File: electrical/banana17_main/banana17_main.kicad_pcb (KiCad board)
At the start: 2 copper layers, 62 parts, among them J1 78171-0004, SW1 SW, SW10 SW, SW11 SW, SW12 SW, SW13 SW, SW14 SW, SW15 SW, SW16 SW, SW17 SW, SW2 SW, SW3 SW, SW4 SW, SW5 SW, SW6 SW, SW7 SW, SW8 SW, SW9 SW, U1 RP2040, U2 NCP1117-3.3_SOT223, U3 ssd1306_128x32, U4 W25Q128JVS, Y1 ABMB-272-T3

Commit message: Minor changes to placement of MCU.
Minor changes to placement of MCU.
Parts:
- moved R3 31.6 mm to (251.0, 101.5)
- moved C1 21.2 mm to (227.4, 114.9)
- moved C10 21.2 mm to (229.6, 114.9)
- moved C4 21.2 mm to (226.4, 114.9)
- moved C8 21.2 mm to (223.3, 122.4)
- moved C9 21.2 mm to (223.3, 118.8)
- moved R2 21.2 mm to (227.9, 111.9)
- moved Y1 21.2 mm to (232.3, 131.0)
- moved C5 21.2 mm to (236.0, 117.7)
- moved C11 21.2 mm to (225.4, 114.9)
- moved C2 21.2 mm to (230.6, 114.9)
- moved C3 21.2 mm to (228.2, 128.5)
- moved C6 21.2 mm to (236.0, 122.4)
- moved C7 21.2 mm to (229.2, 128.5)
- moved J1 21.2 mm to (228.5, 107.7)
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
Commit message: General layout complete.
General layout complete.
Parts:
- C12, C13, C14, C15, C16: footprint Capacitor_SMD:C_0805_2012Metric_Pad1.18x1.45mm_HandSolder -> Capacitor_SMD:C_0402_1005Metric_Pad0.74x0.62mm_HandSolder
- R3: footprint Resistor_SMD:R_0805_2012Metric_Pad1.20x1.40mm_HandSolder -> Resistor_SMD:R_0402_1005Metric_Pad0.72x0.64mm_HandSolder
- moved C13 73.6 mm to (179.8, 87.6)
- moved C12 71.8 mm to (184.3, 87.6), turned to 0 degrees
- moved C16 70.8 mm to (190.1, 114.3), turned to 0 degrees
- moved C15 70.1 mm to (192.8, 114.3)
- moved U2 62.9 mm to (181.4, 92.9), turned to -90 degrees
- moved C14 59.8 mm to (194.2, 90.7)
- moved R3 49.7 mm to (202.6, 90.2)
- moved U4 48.3 mm to (198.4, 94.3)
- moved BOOT_SEL1 46.6 mm to (199.6, 86.3)
- moved J1 43.8 mm to (189.9, 86.8)
- moved Y1 42.9 mm to (191.8, 116.7)
- moved C3 42.3 mm to (189.3, 111.8)
- moved C7 42.3 mm to (190.3, 111.8)
- moved C1 41.9 mm to (188.8, 98.5)
- moved C10 41.9 mm to (191.0, 98.5)
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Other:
- board outline added: 110 x 110 mm

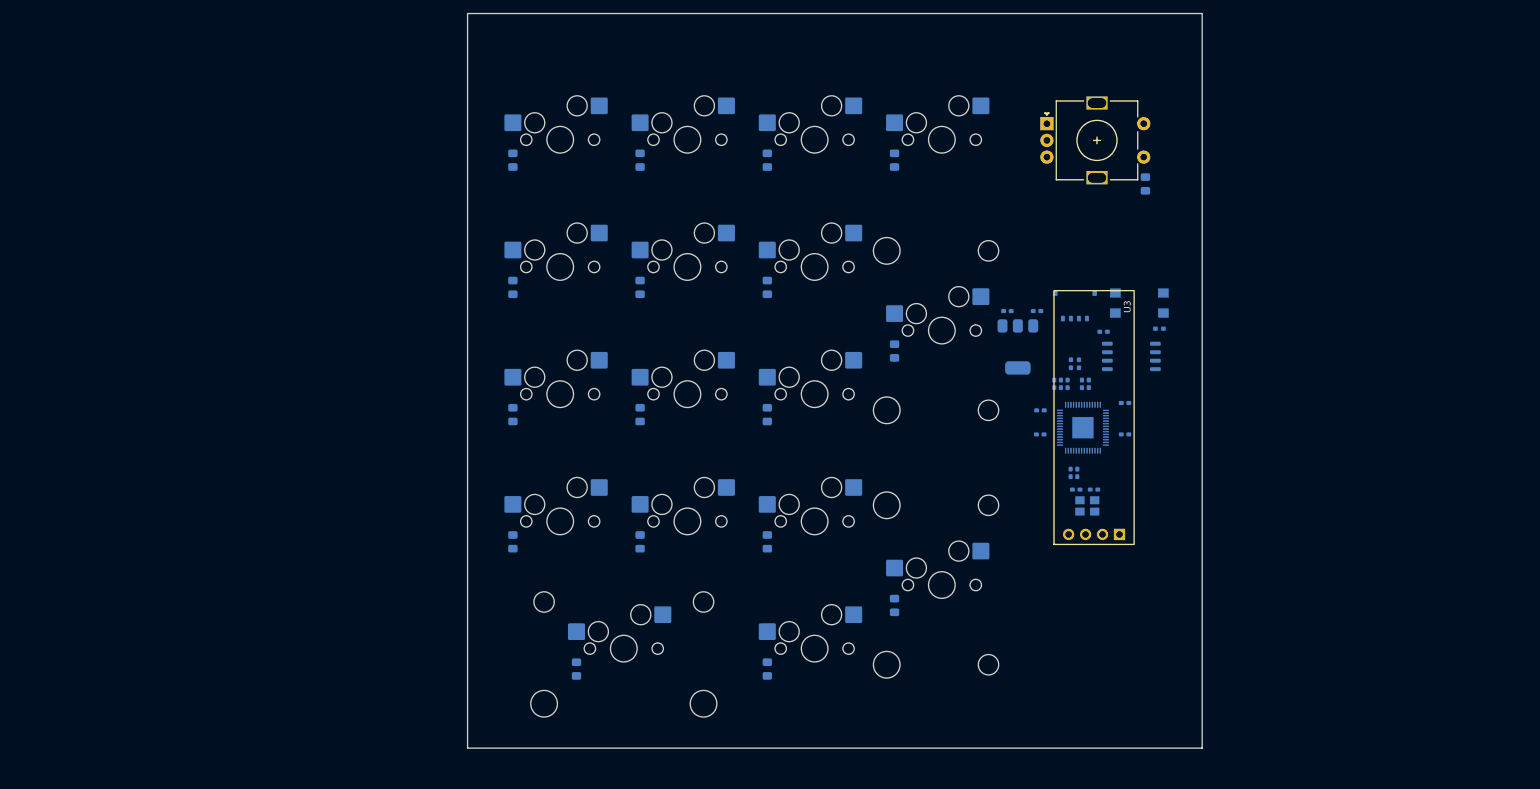
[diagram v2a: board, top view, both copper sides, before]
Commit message: Added second rotary encoder.
Added second rotary encoder.
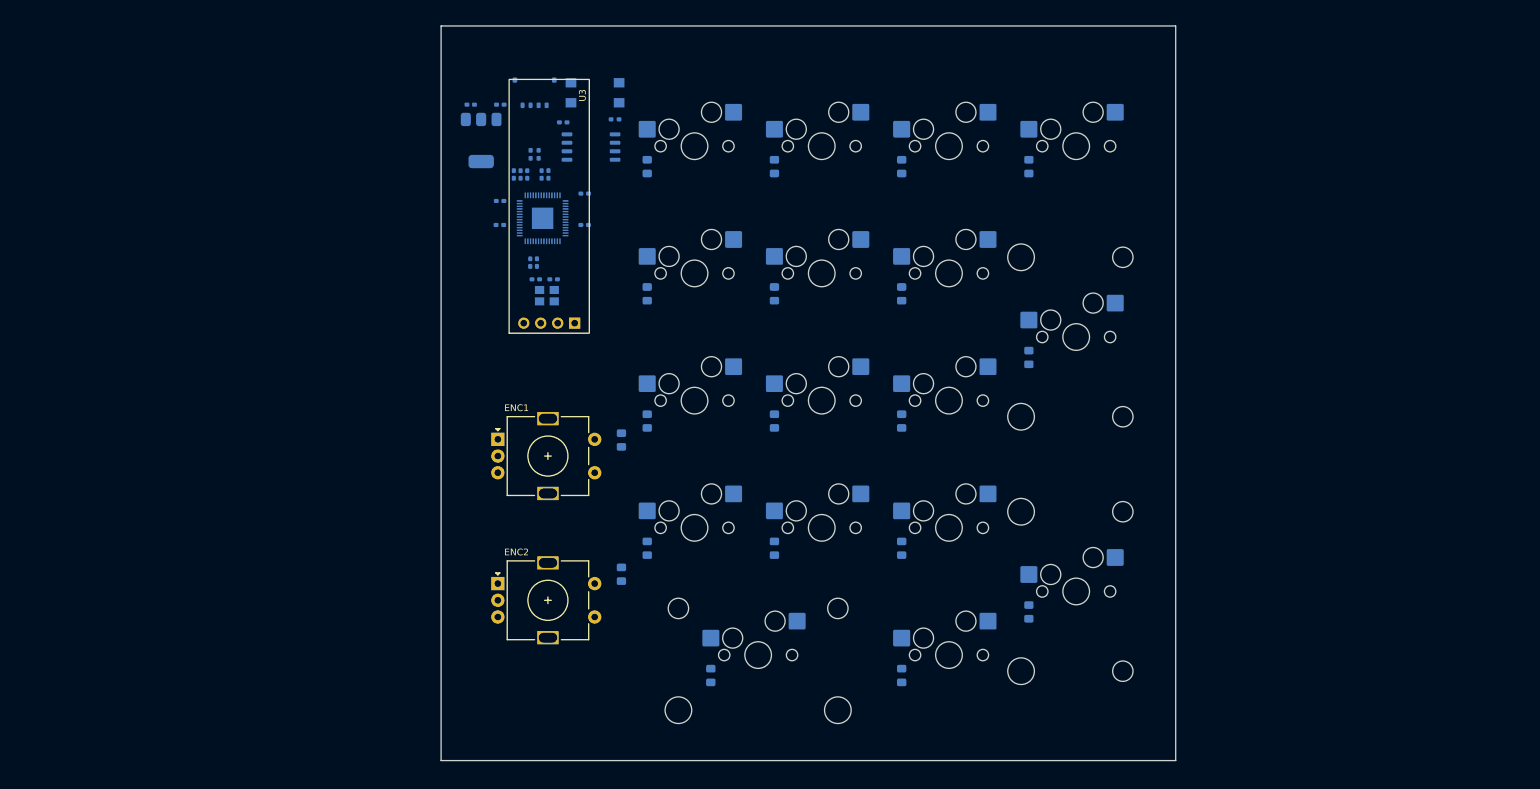
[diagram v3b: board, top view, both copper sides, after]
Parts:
- added ENC2: RotaryEncoder_Switch, Rotary_Encoder:RotaryEncoder_Alps_EC11E-Switch_Vertical_H20mm, F.Cu at (103.5, 128.4)
- added ENC_D2: D, Diode_SMD:D_0805_2012Metric_Pad1.15x1.40mm_HandSolder, B.Cu at (122.0, 127.0)
- moved ENC1 94.8 mm to (103.5, 106.8)
- moved U3 87.5 mm to (111.2, 71.9)
- moved BOOT_SEL1 87.4 mm to (118.1, 54.9)
- moved R3 87.3 mm to (121.1, 58.8)
- moved ENC_D1 87.3 mm to (122.0, 106.9), turned to -90 degrees
- moved J1 87.0 mm to (109.0, 54.9)
- moved C15 86.8 mm to (111.9, 82.8)
- moved C3 86.8 mm to (108.4, 80.3)
- moved C7 86.8 mm to (109.4, 80.3)
- moved Y1 86.8 mm to (110.9, 85.2)
- moved C16 86.8 mm to (109.2, 82.8)
- moved C1 86.8 mm to (107.9, 67.1)
- moved C10 86.8 mm to (110.1, 67.1)
- moved C11 86.8 mm to (105.9, 67.1)
- moved C14 86.8 mm to (113.3, 59.3)
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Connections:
- net ENCODER_A renamed ENC1_B
- net ENCODER_B renamed ENC1_A
- ENC1 pad S2: COL5 -> COL0
- ENC_D1 pad 1: ROW0 -> ROW2
- SW1 pad 2: COL0 -> COL1
- SW10 pad 2: COL1 -> COL2
- SW11 pad 2: COL2 -> COL4
- SW12 pad 2: COL0 -> COL1
- SW13 pad 2: COL1 -> COL2
- SW14 pad 2: COL2 -> COL4
- SW15 pad 2: COL4 -> COL5
- SW16 pad 2: COL1 -> COL2
- SW17 pad 2: COL2 -> COL4
- SW2 pad 2: COL1 -> COL2
- SW3 pad 2: COL2 -> COL4
- SW4 pad 2: COL4 -> COL5
- SW5 pad 2: COL0 -> COL1
- SW6 pad 2: COL1 -> COL2
- SW7 pad 2: COL2 -> COL4
- SW8 pad 2: COL4 -> COL5
- SW9 pad 2: COL0 -> COL1

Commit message: RP2040 routed.
RP2040 routed.
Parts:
- moved U3 74.2 mm to (37.0, 73.7), turned to -90 degrees
- moved BOOT_SEL1 41.0 mm to (102.5, 92.8), turned to 0 degrees
- moved C13 40.0 mm to (119.7, 91.1), turned to 0 degrees
- moved J1 38.1 mm to (111.2, 92.9), turned to 180 degrees
- moved R3 37.4 mm to (98.9, 88.9), turned to 90 degrees
- moved C12 36.6 mm to (116.3, 91.1), turned to 180 degrees
- moved C14 29.9 mm to (106.7, 88.5), turned to 0 degrees
- moved U2 29.9 mm to (119.2, 85.8), turned to 90 degrees
- moved U4 26.5 mm to (102.5, 84.8), turned to 0 degrees
- moved Y1 21.8 mm to (109.3, 63.5), turned to 0 degrees
- moved R2 20.3 mm to (111.7, 84.2), turned to 90 degrees
- moved R1 20.1 mm to (110.5, 84.2), turned to 90 degrees
- moved C15 17.2 mm to (108.2, 66.0), turned to 0 degrees
- moved C16 16.9 mm to (111.0, 66.0), turned to 180 degrees
- moved C11 15.9 mm to (114.3, 80.7), turned to -90 degrees
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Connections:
- net /MCU_DM renamed /MCU_D+
- net /MCU_DP renamed /MCU_D-
- D15 pad 1: ROW3 -> ROW4
- U1 pad 2: /GPIO0 -> ROW0
- U1 pad 3: /GPIO1 -> ROW1
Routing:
- net +3V3: track 0.00 -> 71.3 mm
- net ROW1: track 0.00 -> 61.1 mm
- net ROW0: track 0.00 -> 57.5 mm
- net ROW4: track 0.00 -> 52.6 mm
- net GND: track 0.00 -> 44.9 mm, vias 0 -> 25
- net ROW3: track 0.00 -> 38.1 mm
- net ROW2: track 0.00 -> 38.1 mm
- net +1V1: track 0.00 -> 27.2 mm, vias 0 -> 4
- net /QSPI_SS: track 0.00 -> 21.0 mm
- net /QSPI_SD1: track 0.00 -> 17.8 mm
- net /QSPI_SD2: track 0.00 -> 16.2 mm
- net /QSPI_SD3: track 0.00 -> 9.76 mm
- net /XIN: track 0.00 -> 9.17 mm
- net /~{USB_BOOT}: track 0.00 -> 8.97 mm
- net /QSPI_SCLK: track 0.00 -> 8.35 mm
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- added copper zone on B.Cu, net +3V3
- added copper zone on F.Cu, net GND

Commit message: Incorporated USB C connector. Shrunk overall design.
Incorporated USB C connector. Shrunk overall design.
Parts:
- removed J1: 78171-0004, Connector_Molex:Molex_Pico-EZmate_78171-0004_1x04-1MP_P1.20mm_Vertical
- removed R3: 1k, Resistor_SMD:R_0402_1005Metric_Pad0.72x0.64mm_HandSolder
- added J2: USB_C_Receptacle_USB2.0_16P, locallib:HRO-TYPE-C-31-M-12-Assembly, B.Cu at (105.5, 54.9)
- added R4: 5.1k, Resistor_SMD:R_0402_1005Metric_Pad0.72x0.64mm_HandSolder, B.Cu at (104.2, 65.1)
- added R5: 5.1k, Resistor_SMD:R_0402_1005Metric_Pad0.72x0.64mm_HandSolder, B.Cu at (107.2, 65.1)
- BOOT_SEL1: moved to F.Cu
- moved U3 69.1 mm to (105.6, 82.5), turned to 90 degrees
- moved BOOT_SEL1 37.9 mm to (84.5, 59.4)
- moved C13 34.3 mm to (99.4, 63.5), turned to 180 degrees
- moved Y1 27.4 mm to (107.8, 90.9), turned to 180 degrees
- moved C12 26.4 mm to (104.2, 67.7), turned to -90 degrees
- moved U2 25.7 mm to (100.0, 68.6), turned to -90 degrees
- moved C16 23.0 mm to (106.1, 88.5), turned to 0 degrees
- moved C15 22.5 mm to (108.9, 88.5), turned to 180 degrees
- moved C7 19.6 mm to (106.1, 86.7), turned to -135 degrees
- moved C14 18.9 mm to (107.8, 69.7), turned to 90 degrees
- moved C3 18.6 mm to (105.3, 86.0), turned to -135 degrees
- moved U4 18.4 mm to (111.4, 68.7), turned to -90 degrees
- moved C8 17.7 mm to (100.7, 81.4), turned to 180 degrees
- moved R2 14.5 mm to (105.3, 71.2), turned to -90 degrees
- moved C9 13.6 mm to (101.8, 76.5), turned to 135 degrees
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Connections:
- U1 pad 4: /GPIO2 -> ROW2
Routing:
- net GND: track 44.9 -> 25.6 mm, vias 25 -> 20
- net /~{USB_BOOT}: track 8.97 -> 0.00 mm
- net +3V3: track 71.3 -> 65.5 mm
- net /QSPI_SD3: track 9.76 -> 5.95 mm
- net /QSPI_SD1: track 17.8 -> 21.5 mm
- net /QSPI_SD2: track 16.2 -> 19.5 mm
- net +1V1: track 27.2 -> 24.2 mm
- net /QSPI_SS: track 21.0 -> 23.8 mm
- net Net-(J2-CC1): track 0.00 -> 1.92 mm
- net Net-(J2-CC2): track 0.00 -> 1.90 mm
- net /QSPI_SCLK: track 8.35 -> 6.56 mm
- net VBUS: track 7.48 -> 5.78 mm
- net /USB_D-: track 6.57 -> 8.18 mm
- net /USB_D+: track 6.58 -> 8.12 mm
- net /MCU_D-: track 6.20 -> 5.32 mm
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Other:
- board outline removed

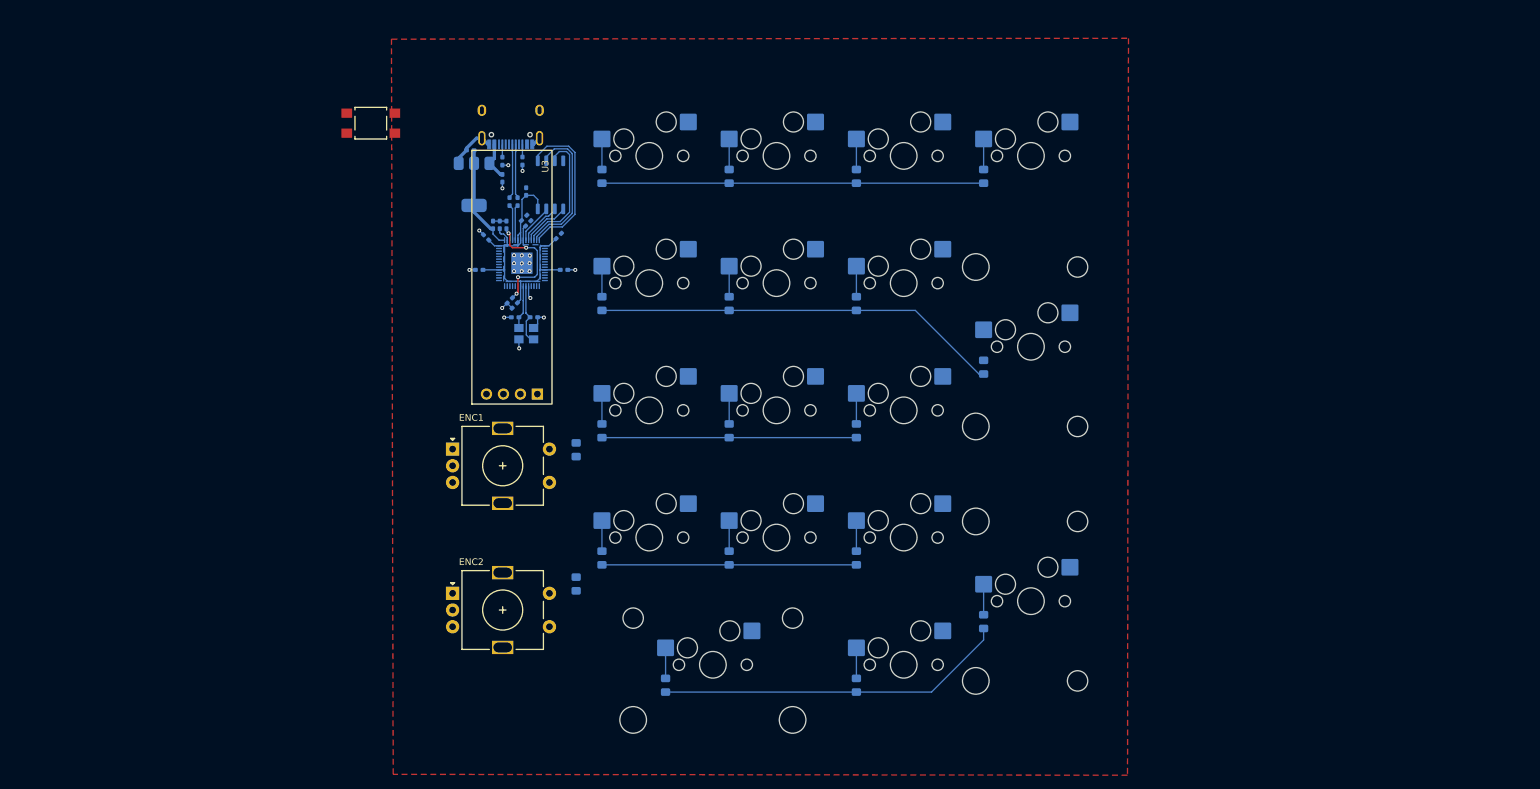
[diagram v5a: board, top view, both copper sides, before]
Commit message: Preliminary matrix complete. Need to do encoders next.
Preliminary matrix complete. Need to do encoders next.
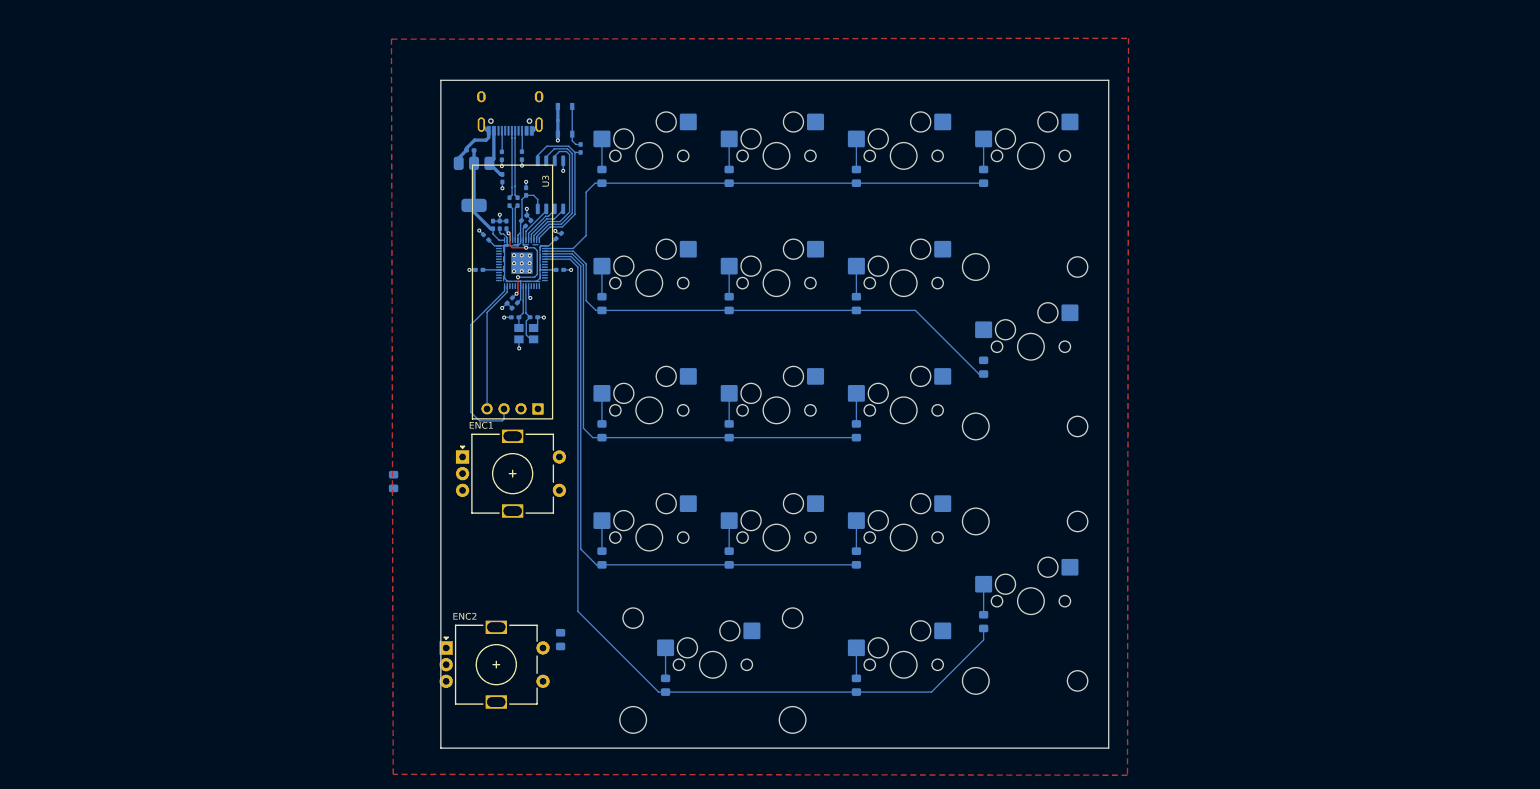
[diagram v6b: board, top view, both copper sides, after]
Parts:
- added R5: 1k, Resistor_SMD:R_0402_1005Metric_Pad0.72x0.64mm_HandSolder, B.Cu at (115.9, 63.2)
- BOOT1: renamed from BOOT_SEL1; footprint Button_Switch_SMD:SW_SPST_TL3305A -> Button_Switch_SMD:SW_SPST_PTS810; moved to B.Cu
- moved BOOT1 29.1 mm to (113.6, 59.0), turned to -90 degrees
- moved ENC_D1 27.7 mm to (87.9, 113.1)
- moved ENC_D2 8.65 mm to (112.9, 136.8)
- moved ENC2 8.24 mm to (95.8, 138.0)
- moved U3 2.22 mm to (105.7, 84.7)
- moved J1 2.03 mm to (105.4, 52.9)
- moved ENC1 1.90 mm to (98.2, 109.4)
- moved R3 0.80 mm to (104.1, 64.3)
- moved R4 0.80 mm to (107.1, 64.3)
- moved C6 0.62 mm to (112.8, 81.4)
- renumbered D16 to D15, D17 to D16, D15 to D17, J2 to J1, R4 to R3, R5 to R4, SW16 to SW15, SW17 to SW16, SW15 to SW17
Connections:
- U1 pad 27: /GPIO16 -> OLED_SDA
- U1 pad 28: /GPIO17 -> OLED_SCL
- U1 pad 5: /GPIO3 -> ROW3
- U1 pad 6: /GPIO4 -> ROW4
- U3 pad 4: OLED_GND -> GND
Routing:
- net ROW4: track 52.6 -> 127.7 mm
- net ROW3: track 38.1 -> 90.6 mm
- net ROW2: track 38.1 -> 72.4 mm
- net OLED_SCL: track 0.00 -> 28.1 mm
- net OLED_SDA: track 0.00 -> 19.6 mm
- net ROW0: track 57.5 -> 73.6 mm
- net ROW1: track 61.1 -> 76.5 mm
- net GND: track 25.6 -> 39.1 mm, vias 20 -> 26
- net /~{USB_BOOT}: track 0.00 -> 6.63 mm
- net /USB_D+: track 8.12 -> 10.2 mm
- net /USB_D-: track 8.18 -> 10.2 mm
- net VBUS: track 5.78 -> 7.78 mm
- net Net-(J1-CC2): track 1.90 -> 3.14 mm
- net Net-(J1-CC1): track 1.92 -> 3.15 mm
- net /QSPI_SS: track 23.8 -> 24.6 mm
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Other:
- board outline added: 100 x 100 mm

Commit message: Initial PCB complete.
Initial PCB complete.
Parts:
- moved ENC_D1 26.5 mm to (112.5, 122.8), turned to 90 degrees
- moved ENC_D2 7.68 mm to (112.5, 144.4), turned to 90 degrees
- moved ENC2 5.57 mm to (98.0, 132.9)
- moved U3 2.22 mm to (105.6, 82.5)
- moved ENC1 1.91 mm to (98.0, 111.3)
- moved C6 0.82 mm to (112.8, 82.2), turned to -45 degrees
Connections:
- ENC2 pad S2: COL0 -> ROW5
- ENC_D1 pad 1: ROW2 -> ROW5
- ENC_D2 pad 1: ROW3 -> ROW6
- SW11 pad 2: COL4 -> COL3
- SW14 pad 2: COL4 -> COL3
- SW16 pad 2: COL4 -> COL3
- SW17 pad 2: COL5 -> COL4
- SW3 pad 2: COL4 -> COL3
- SW4 pad 2: COL5 -> COL4
- SW7 pad 2: COL4 -> COL3
- SW8 pad 2: COL5 -> COL4
- U1 pad 12: /GPIO9 -> ROW6
- U1 pad 13: /GPIO10 -> ROW5
- U1 pad 14: /GPIO11 -> COL0
- U1 pad 15: /GPIO12 -> OLED_SDA
- U1 pad 16: /GPIO13 -> OLED_SCL
- U1 pad 27: OLED_SDA -> /GPIO16
- U1 pad 28: OLED_SCL -> /GPIO17
- U1 pad 31: /GPIO20 -> ENC1_A
- U1 pad 32: /GPIO21 -> ENC1_B
- U1 pad 5: ROW3 -> COL1
- U1 pad 6: ROW4 -> COL2
- U1 pad 7: /GPIO5 -> COL3
- U1 pad 8: /GPIO6 -> COL4
- U3 pad 3: OLED_VCC -> VBUS
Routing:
- net COL4: track 0.00 -> 250.0 mm, vias 0 -> 4
- net COL3: track 0.00 -> 233.3 mm, vias 0 -> 6
- net COL2: track 0.00 -> 222.6 mm, vias 0 -> 6
- net COL1: track 0.00 -> 102.4 mm, vias 0 -> 5
- net ROW4: track 127.7 -> 53.0 mm
- net ROW6: track 0.00 -> 66.7 mm
- net ENC2_B: track 0.00 -> 57.8 mm
- net ROW5: track 0.00 -> 53.2 mm
- net ENC2_A: track 0.00 -> 52.6 mm
- net ROW3: track 90.6 -> 38.1 mm
- net VBUS: track 7.78 -> 50.3 mm, vias 0 -> 1
- net ENC1_B: track 0.00 -> 40.3 mm
- net ENC1_A: track 0.00 -> 33.7 mm
- net COL0: track 0.00 -> 29.6 mm
- net OLED_SDA: track 19.6 -> 30.4 mm
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
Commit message: Incorporated switch step files.
Incorporated switch step files.
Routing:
- net VBUS: track 50.3 -> 57.2 mm
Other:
- outline, holes or cut-outs redrawn
